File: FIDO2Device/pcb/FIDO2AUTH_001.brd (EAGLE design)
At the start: 25.4 x 30.5 mm, 15 parts, among them CN1 TE-1734028, U1 MDBT50Q-P1M, X1 NX3215SA-32.768K

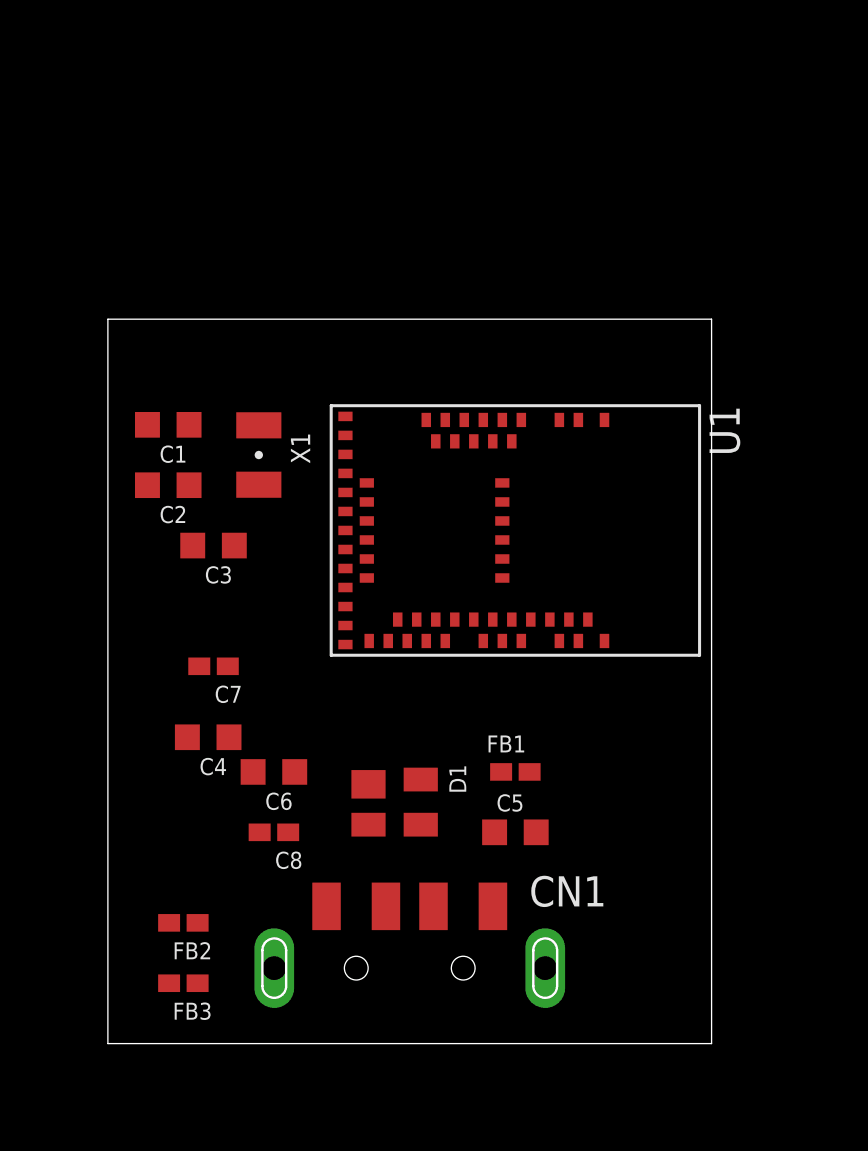
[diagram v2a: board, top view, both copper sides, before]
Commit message: [WIP] ブレークアウト基板回路図
・リセット回路、MAIN SWを追加
・回路図プレビュー、プリント基板配置イメージを追加
・電源供給／プログラミング／GPIOの各ピンをインターフェースするための機構は後日追加予定です。
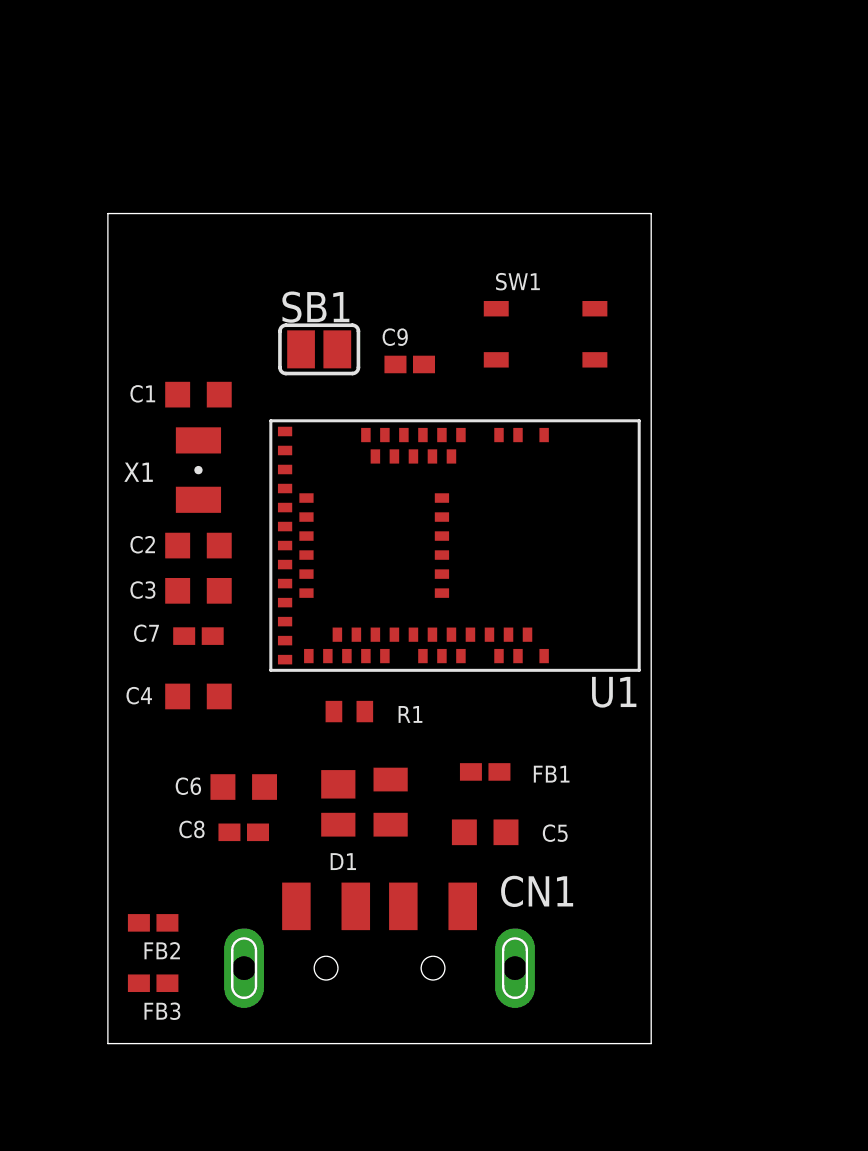
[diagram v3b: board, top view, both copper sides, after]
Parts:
- added C9: 0.1uF, Parts:C0402K
- added R1: 10k, Parts:R0402
- added SB1: (no value), Connectors:SJ
- added SW1: SKRPACE010, Parts:SKRPACE010
- FB1, FB2, FB3: device Parts:C0402K -> Parts:C0402K@1
- moved C2 2.84 mm to (3.81, 21.0)
- moved X1 2.62 mm to (3.81, 24.1)
- moved U1 2.62 mm to (14.6, 21.0)
- moved C3 2.01 mm to (3.81, 19.1)
- moved C1 1.80 mm to (3.81, 27.3)
- moved C4 1.76 mm to (3.81, 14.6)
- moved C6 1.42 mm to (5.71, 10.8)
- moved C7 1.42 mm to (3.81, 17.1)
- moved C8 1.27 mm to (5.71, 8.89)
- moved FB2 1.27 mm to (1.91, 5.08)
- moved FB3 1.27 mm to (1.91, 2.54)
- moved C5 1.27 mm to (15.9, 8.89)
- moved CN1 1.27 mm to (11.4, 3.17)
- moved D1 1.27 mm to (10.8, 10.2)
- moved FB1 1.27 mm to (15.9, 11.4)
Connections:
- new net LED1: U1.22
- new net LED2_B: U1.29
- new net LED2_G: U1.26
- new net LED2_R: U1.24
- new net SW1: SW1.1, SW1.2, U1.57
- net 0V: now also C9.2, SB1.1, SW1.3, SW1.4
- net RESET: now also C9.1, R1.2, SB1.2
- net VDD_NRF: now also R1.1
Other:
- board size 25.4 x 30.5 mm -> 22.9 x 34.9 mm

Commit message: [WIP] ブレークアウト基板回路図
・リセット回路を、ジャンパーではなく超小型タクトスイッチに置換え
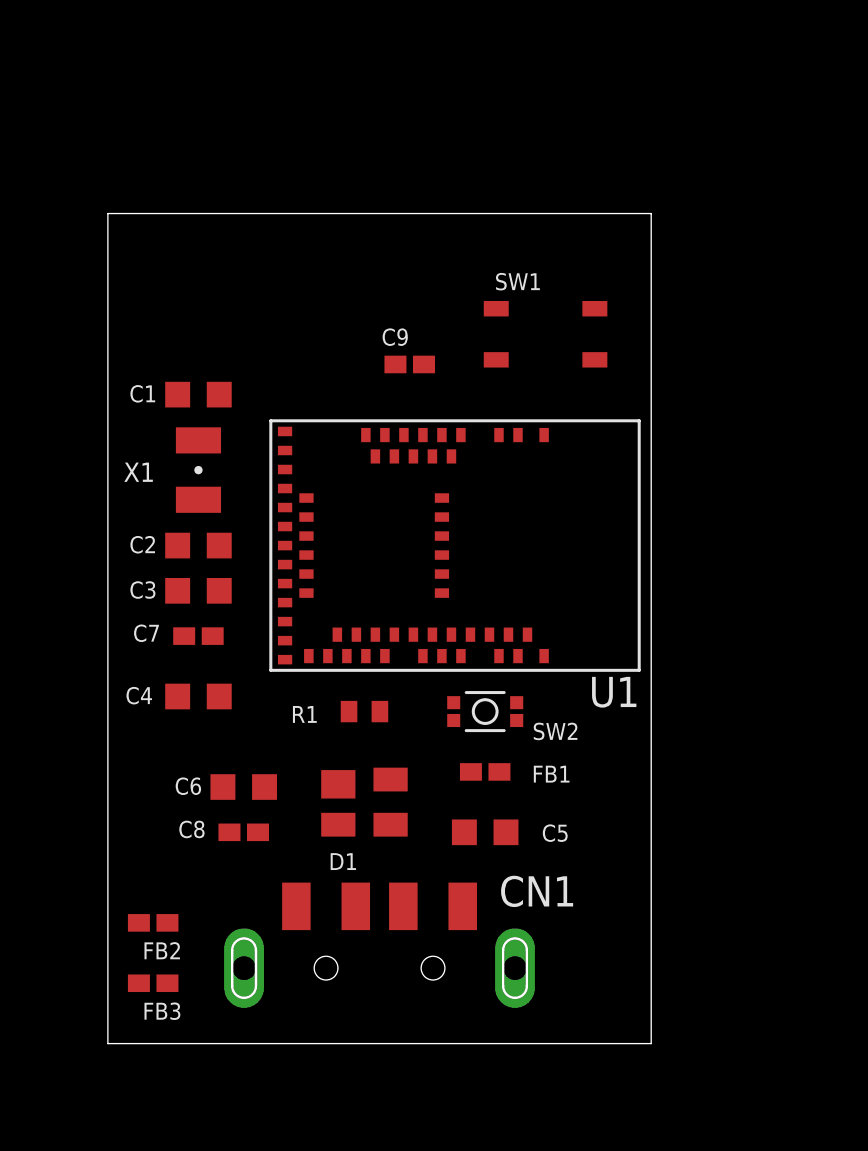
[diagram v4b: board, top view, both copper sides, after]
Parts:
- removed SB1: (no value), Connectors:SJ
- added SW2: SKTADAE010, Parts:SKTADAE010
- moved R1 0.63 mm to (10.8, 14.0)
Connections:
- net 0V: now also SW2.1, SW2.3; no longer SB1.1
- net RESET: now also SW2.2, SW2.4; no longer SB1.2
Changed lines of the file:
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@@
 <attribute name="VALUE" x="6.93" y="-1.325" size="1.27" layer="27"/>
 </element>
-<element name="R1" library="Parts" package="R0402" value="10k" x="10.16" y="13.97" smashed="yes">
-<attribute name="NAME" x="12.144375" y="13.49375" size="0.7112" layer="25"/>
-<attribute name="VALUE" x="9.604375" y="12.54125" size="0.7112" layer="27"/>
+<element name="R1" library="Parts" package="R0402" value="10k" x="10.795" y="13.97" smashed="yes">
+<attribute name="NAME" x="7.699375" y="13.49375" size="0.7112" layer="25"/>
+<attribute name="VALUE" x="10.239375" y="12.54125" size="0.7112" layer="27"/>
 </element>
 <element name="C9" library="Parts" package="C0402K" value="0.1uF" x="12.7" y="28.575"/>
-<element name="SB1" library="Connectors" package="SJ" value="" x="8.89" y="29.21"/>
 <element name="SW1" library="Parts" package="SKRPACE010" value="SKRPACE010" x="18.415" y="29.845"/>
+<element name="SW2" library="Parts" package="SKTADAE010" value="SKTADAE010" x="15.875" y="13.97" smashed="yes" rot="R180">
+<attribute name="NAME" x="17.859375" y="12.779375" size="0.7112" layer="25" ratio="11"/>
+<attribute name="VALUE" x="17.224375" y="15.255875" size="0.7112" layer="27" ratio="11" rot="R180" align="top-left"/>
+</element>
 </elements>
 <signals>
@@
 <contactref element="C6" pad="2"/>
 <contactref element="C9" pad="2"/>
-<contactref element="SB1" pad="1"/>
 <contactref element="SW1" pad="3"/>
 <contactref element="SW1" pad="4"/>
+<contactref element="SW2" pad="3"/>
+<contactref element="SW2" pad="1"/>
 <wire x1="18.355" y1="25.605" x2="20.49" y2="28.77" width="0" layer="19" extent="1-1"/>
 <wire x1="17.255" y1="25.605" x2="18.355" y2="25.605" width="0" layer="19" extent="1-1"/>
-<wire x1="16.34" y1="28.77" x2="20.49" y2="28.77" width="0" layer="19" extent="1-1"/>
+<wire x1="16.34" y1="28.77" x2="17.255" y2="25.605" width="0" layer="19" extent="1-1"/>
 <wire x1="13.3" y1="28.575" x2="16.34" y2="28.77" width="0" layer="19" extent="1-1"/>
 <wire x1="7.455" y1="25.755" x2="13.3" y2="28.575" width="0" layer="19" extent="1-1"/>
 <wire x1="2.935" y1="27.305" x2="7.455" y2="25.755" width="0" layer="19" extent="1-1"/>
-<wire x1="8.128" y1="29.21" x2="2.935" y2="27.305" width="0" layer="19" extent="1-1"/>
 <wire x1="2.935" y1="20.955" x2="2.935" y2="27.305" width="0" layer="19" extent="1-1"/>
 <wire x1="2.935" y1="19.05" x2="2.935" y2="20.955" width="0" layer="19" extent="1-1"/>
 <wire x1="3.21" y1="17.145" x2="2.935" y2="19.05" width="0" layer="19" extent="1-1"/>
 <wire x1="2.935" y1="14.605" x2="3.21" y2="17.145" width="0" layer="19" extent="1-1"/>
-<wire x1="7.455" y1="16.155" x2="3.21" y2="17.145" width="0" layer="19" extent="1-1"/>
 <wire x1="4.84" y1="10.795" x2="2.935" y2="14.605" width="0" layer="19" extent="1-1"/>
 <wire x1="5.115" y1="8.89" x2="4.84" y2="10.795" width="0" layer="19" extent="1-1"/>
+<wire x1="7.455" y1="16.155" x2="3.21" y2="17.145" width="0" layer="19" extent="1-1"/>
 <wire x1="9.695" y1="10.91" x2="4.84" y2="10.795" width="0" layer="19" extent="1-1"/>
 <wire x1="1.305" y1="5.08" x2="5.115" y2="8.89" width="0" layer="19" extent="1-1"/>
 <wire x1="1.305" y1="2.54" x2="1.305" y2="5.08" width="0" layer="19" extent="1-1"/>
 <wire x1="16.75" y1="8.89" x2="9.695" y2="10.91" width="0" layer="19" extent="1-1"/>
-<wire x1="18.355" y1="16.305" x2="16.75" y2="8.89" width="0" layer="19" extent="1-1"/>
+<wire x1="17.2" y1="13.595" x2="16.75" y2="8.89" width="0" layer="19" extent="1-1"/>
+<wire x1="17.2" y1="14.345" x2="17.2" y2="13.595" width="0" layer="19" extent="1-1"/>
+<wire x1="18.355" y1="16.305" x2="17.2" y2="14.345" width="0" layer="19" extent="1-1"/>
 </signal>
 <signal name="XL1">
@@
 <contactref element="C2" pad="1"/>
 <contactref element="U1" pad="18"/>
-<wire x1="4.685" y1="20.955" x2="7.455" y2="23.355" width="0" layer="19" extent="1-1"/>
-<wire x1="3.81" y1="22.88" x2="4.685" y2="20.955" width="0" layer="19" extent="1-1"/>
+<wire x1="3.81" y1="22.88" x2="7.455" y2="23.355" width="0" layer="19" extent="1-1"/>
+<wire x1="4.685" y1="20.955" x2="3.81" y2="22.88" width="0" layer="19" extent="1-1"/>
 </signal>
 <signal name="VBUS_NRF">
@@
 <contactref element="R1" pad="2"/>
 <contactref element="C9" pad="1"/>
-<contactref element="SB1" pad="2"/>
-<wire x1="9.652" y1="29.21" x2="12.1" y2="28.575" width="0" layer="19" extent="1-1"/>
+<contactref element="SW2" pad="2"/>
+<contactref element="SW2" pad="4"/>
 <wire x1="11.255" y1="17.205" x2="12.1" y2="28.575" width="0" layer="19" extent="1-1"/>
-<wire x1="10.81" y1="13.97" x2="11.255" y2="17.205" width="0" layer="19" extent="1-1"/>
+<wire x1="11.445" y1="13.97" x2="11.255" y2="17.205" width="0" layer="19" extent="1-1"/>
+<wire x1="14.55" y1="13.595" x2="11.445" y2="13.97" width="0" layer="19" extent="1-1"/>
+<wire x1="14.55" y1="14.345" x2="14.55" y2="13.595" width="0" layer="19" extent="1-1"/>
 </signal>
 <signal name="D_P">
@@
 <wire x1="7.455" y1="18.555" x2="7.455" y2="19.355" width="0" layer="19" extent="1-1"/>
 <wire x1="4.685" y1="19.05" x2="7.455" y2="19.355" width="0" layer="19" extent="1-1"/>
-<wire x1="9.51" y1="13.97" x2="7.455" y2="18.555" width="0" layer="19" extent="1-1"/>
+<wire x1="10.145" y1="13.97" x2="7.455" y2="18.555" width="0" layer="19" extent="1-1"/>
 </signal>
 <signal name="N$1">

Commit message: [WIP] ブレークアウト基板回路図
・LED２点配置
・リセットスイッチ配置
・各部品の配置を見直し
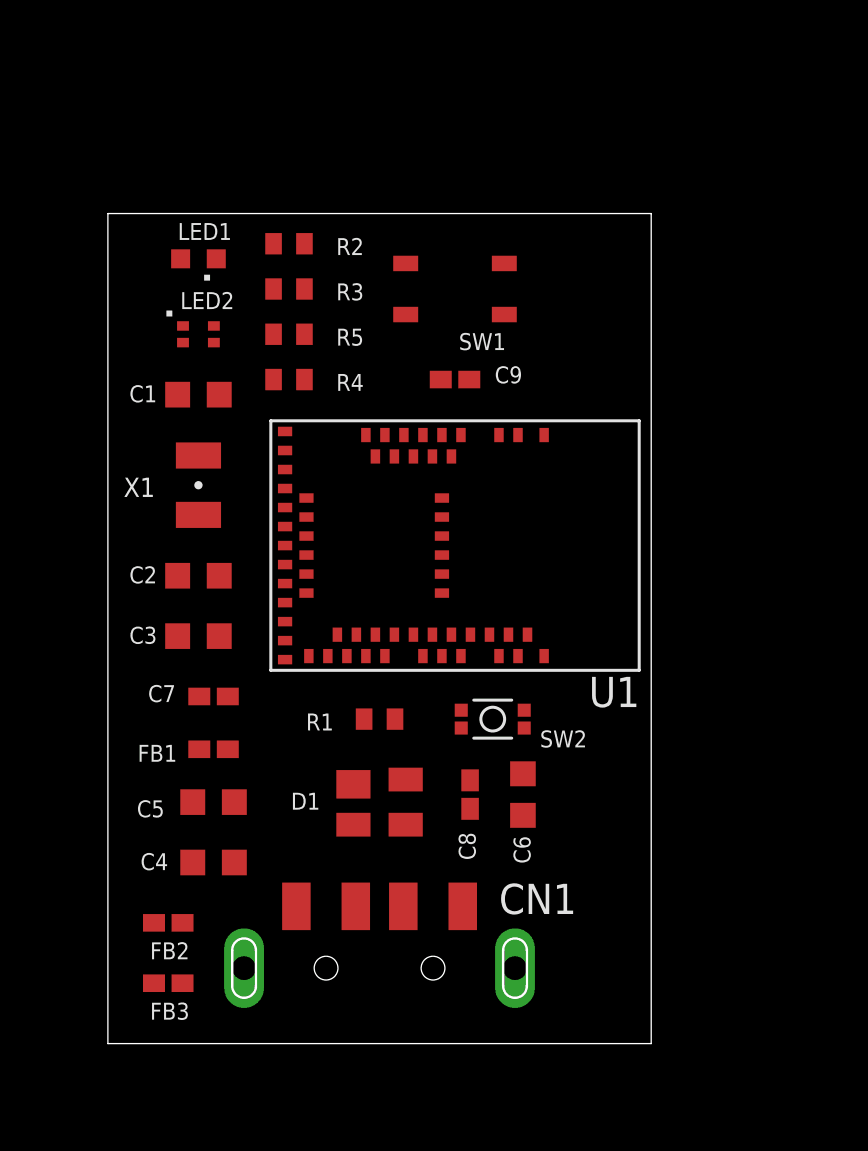
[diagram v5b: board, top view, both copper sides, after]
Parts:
- added LED1: APHD1608LSURCK, Parts:CHIPLED_0603
- added LED2: APHF1608LSEEQBDZGKC, Parts:APHF1608LSEEQBDZGKC
- added R2: 1.5k, Parts:R0402
- added R3: 1.2k, Parts:R0402
- added R4: 2.2k, Parts:R0402
- added R5: 390, Parts:R0402
- moved C6 11.8 mm to (17.5, 10.5), turned to 270 degrees
- moved C5 11.5 mm to (4.45, 10.2), turned to 180 degrees
- moved FB1 11.5 mm to (4.45, 12.4)
- moved C8 9.66 mm to (15.2, 10.5), turned to 270 degrees
- moved C4 7.01 mm to (4.45, 7.62)
- moved SW1 4.26 mm to (14.6, 31.8), turned to 180 degrees
- moved C7 2.62 mm to (4.45, 14.6)
- moved C9 2.01 mm to (14.6, 27.9)
- moved C3 1.91 mm to (3.81, 17.1)
- moved C2 1.27 mm to (3.81, 19.7)
- moved R1 0.71 mm to (11.4, 13.7)
- moved FB2 0.64 mm to (2.54, 5.08)
- moved FB3 0.64 mm to (2.54, 2.54)
- moved D1 0.63 mm to (11.4, 10.2)
- moved X1 0.63 mm to (3.81, 23.5)
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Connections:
- net N$1 renamed VBUS
- removed net NFC1: U1.52
- removed net NFC2: U1.54
- new net N$10: LED2.4, R5.2
- new net N$11: LED1.C, R2.2
- new net N$8: LED2.2, R3.2
- new net N$9: LED2.3, R4.2
- net LED1: now also R2.1
- net LED2_B: now also R5.1
- net LED2_G: now also R4.1
- net LED2_R: now also R3.1
- net VDD_NRF: now also LED1.A, LED2.1
